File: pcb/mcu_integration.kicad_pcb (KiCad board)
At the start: 4 copper layers, 70 x 70 mm, 73 parts, among them IC1 TL7660IDGKR, IC2 TL081IDT, IC6 AD844_OPAMP_AL, IC7 FOD814_OPTO_AL, J1 Conn_01x05, J5 DM3BT-DSF-PEJS, M1 MountingHole_Pad, M2 MountingHole_Pad, M3 MountingHole_Pad, M4 MountingHole_Pad, U1 STM32F103RBTx, U2 LTC4300A-1IMS8_PBF, U3 REF192_AL, U6 LM35DM

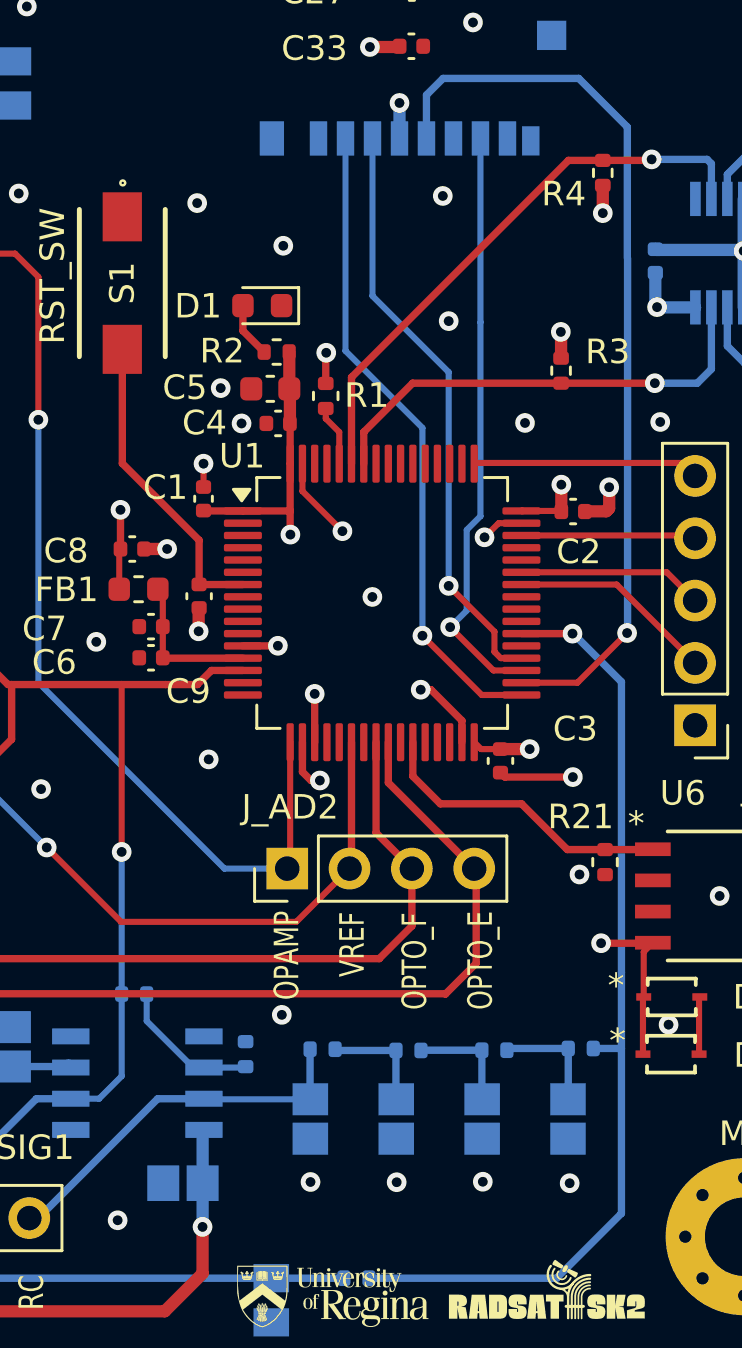
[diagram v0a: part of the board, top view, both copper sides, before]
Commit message: Added capacitor to op amp circuit
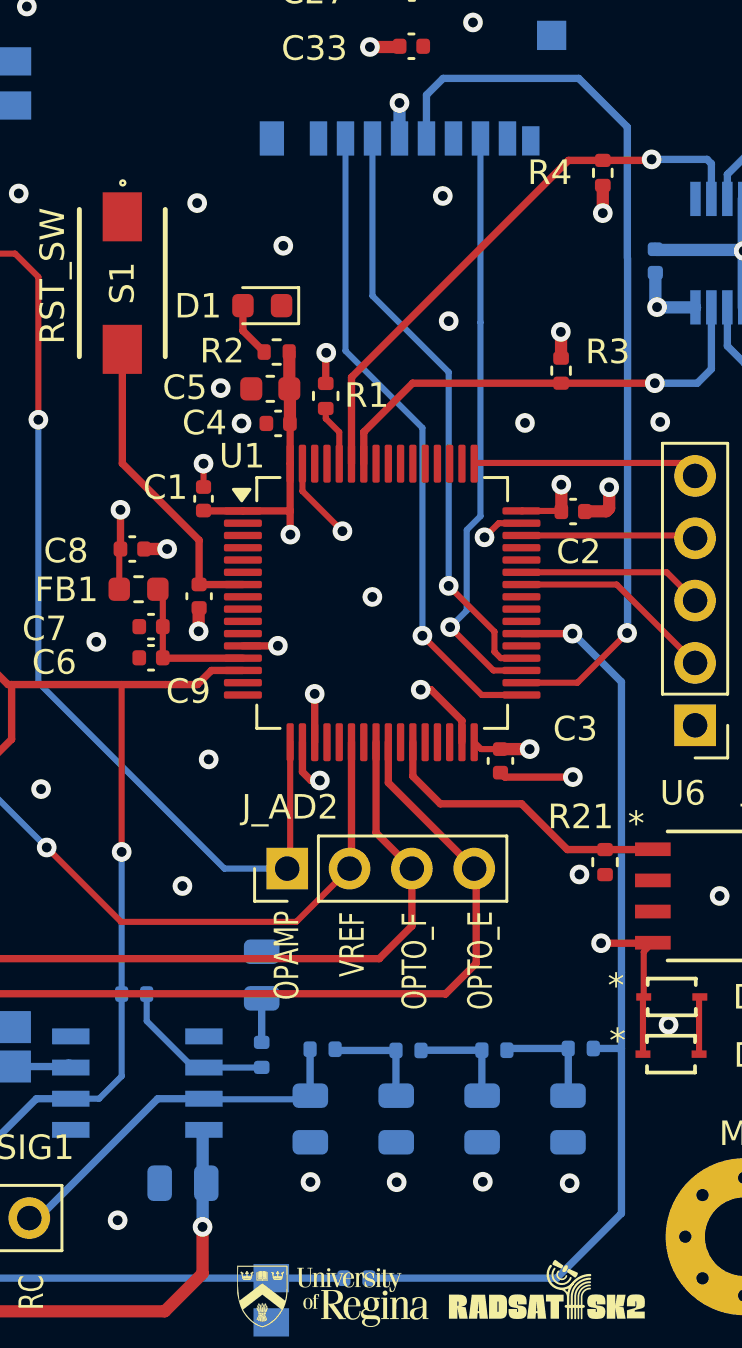
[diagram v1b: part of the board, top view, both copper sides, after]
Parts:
- added C47: 4.7u, Capacitor_SMD:C_0805_2012Metric, B.Cu at (153.6, 114.0)
- C14, C15, C16, C17, C18: footprint capstone:CAPC220145_88N_KEM-0.1u -> Capacitor_SMD:C_0805_2012Metric
- moved R9 0.66 mm to (153.6, 117.3)
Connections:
- R9 pad 2: GND -> Net-(C47-Pad1)
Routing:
- net Net-(C47-Pad1): track 0.00 -> 2.08 mm
- net Net-(IC2-INVERTING_INPUT): track 5.93 -> 6.52 mm
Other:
- board text added: "Minature Analog Payload REV B Owen Markewich Hunter Gerbrandt"
- board text removed: "Minature Analog Payload REV A Owen Markewich Hunter Gerbrandt"

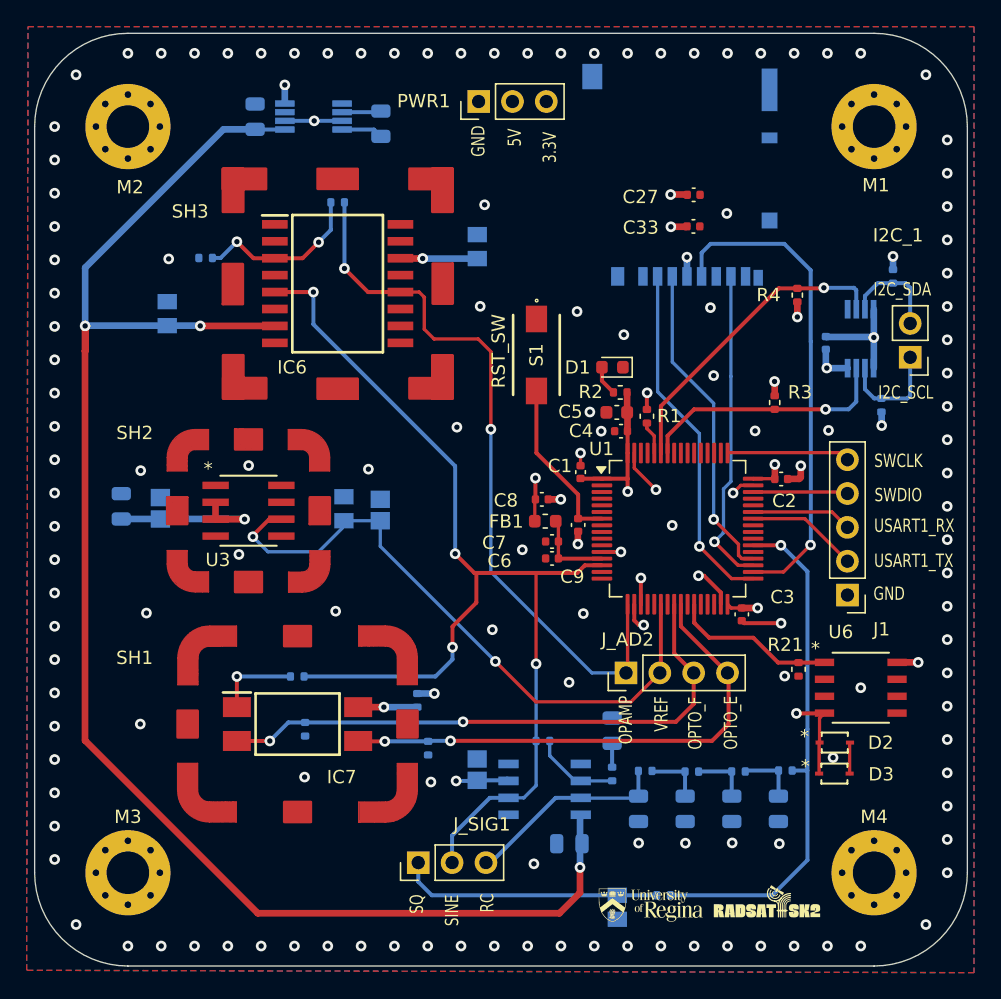
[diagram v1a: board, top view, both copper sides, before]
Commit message: Added switchable input for opto-coupler
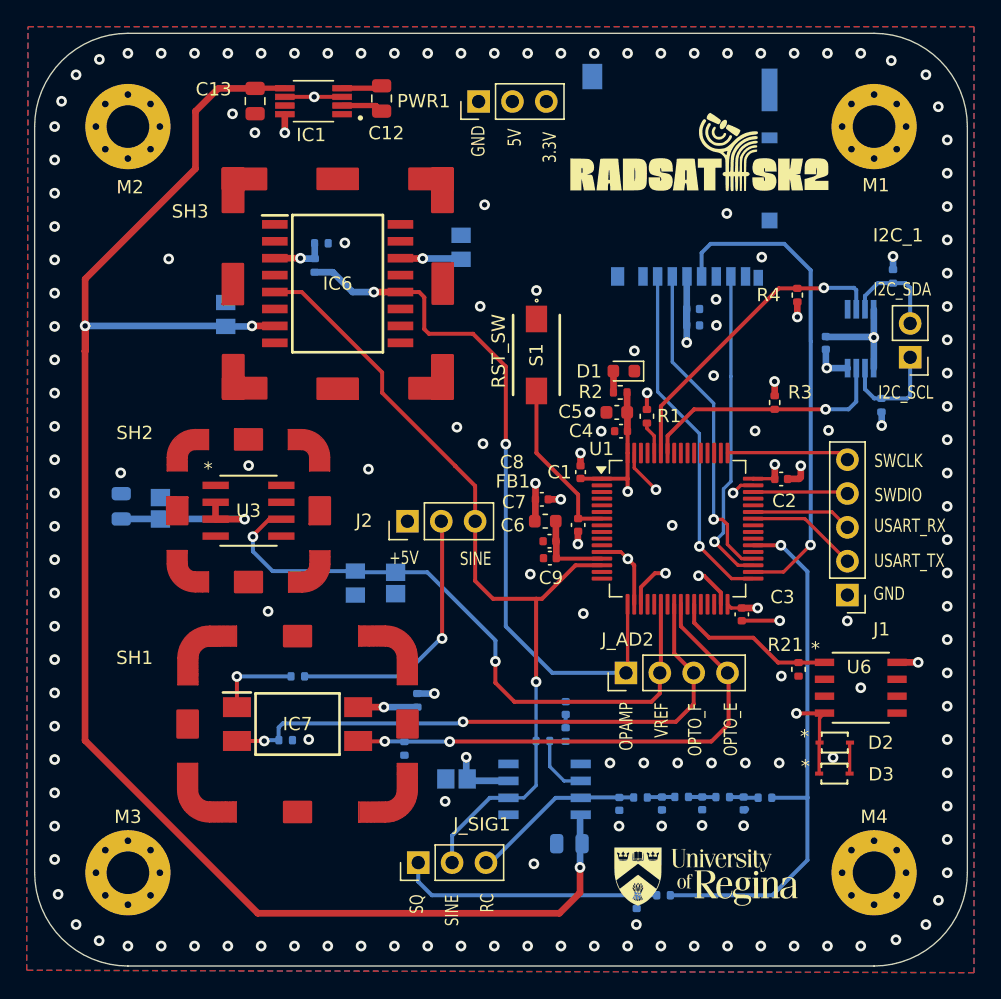
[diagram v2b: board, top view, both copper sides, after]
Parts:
- added G***: LOGO, LOGO, F.Cu at (160.0, 70.8)
- added G***: LOGO, LOGO, F.Cu at (160.6, 125.0)
- added J2: Conn_01x03, Connector_PinHeader_2.54mm:PinHeader_1x03_P2.54mm_Vertical, F.Cu at (138.2, 98.3)
- C12, C13, IC1: moved to F.Cu
- C14, C15, C16, C17, C47: footprint Capacitor_SMD:C_0805_2012Metric -> Capacitor_SMD:C_0402_1005Metric
- C27, C33: moved to B.Cu
- C43: footprint capstone:C0805 -> Capacitor_SMD:C_0402_1005Metric
- moved C27 9.80 mm to (159.6, 83.6)
- moved R22 8.76 mm to (131.7, 77.5), turned to 180 degrees
- moved C33 6.20 mm to (159.6, 82.4)
- moved C31 5.65 mm to (134.3, 103.0), turned to -90 degrees
- moved C32 5.59 mm to (137.3, 103.0), turned to -90 degrees
- moved R25 5.03 mm to (131.2, 79.1), turned to 90 degrees
- moved R9 4.58 mm to (150.1, 114.3)
- moved C29 4.39 mm to (124.6, 82.8)
- moved C47 3.87 mm to (150.1, 112.3)
- moved C14 2.64 mm to (163.4, 119.5)
- moved R5 2.55 mm to (165.0, 119.1)
- moved C15 2.26 mm to (160.3, 119.5)
- moved R6 2.25 mm to (161.9, 119.0)
- moved R7 2.05 mm to (158.8, 119.0)
- moved R8 2.02 mm to (155.7, 119.0)
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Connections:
- R23 pad 2: ADC1_IN0_SINE -> Net-(J2-Pin_2)
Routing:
- net Net-(J2-Pin_2): track 0.00 -> 20.6 mm, vias 0 -> 1
- net ADC1_IN0_SINE: track 84.6 -> 65.2 mm, vias 4 -> 1
- net Net-(IC6--IN): track 12.9 -> 4.16 mm, vias 2 -> 1
- net 3.3V Output: track 44.0 -> 48.2 mm, vias 13 -> 11
- net -5V Output: track 119.9 -> 123.2 mm
- net Net-(C14-Pad1): track 4.60 -> 2.17 mm
- net Net-(C15-Pad1): track 4.49 -> 2.06 mm
- net Net-(C16-Pad1): track 4.49 -> 2.09 mm
- net RC_OUTPUT: track 16.0 -> 13.8 mm
- net GND: track 35.3 -> 37.4 mm, vias 145 -> 161
- net SIG_SQUARE: track 39.1 -> 40.6 mm
- net ADC1_IN3_OPAMP_AL: track 55.8 -> 54.7 mm
- net Net-(C47-Pad1): track 2.08 -> 1.00 mm
- net ADC1_IN14_OPTO_F_AL: track 43.5 -> 44.2 mm
- net Net-(D1-A): track 2.25 -> 1.60 mm
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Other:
- board text added: "+5V"
- board text added: "USART_RX"
- board text added: "USART_TX"
- board text removed: "USART1_RX"
- board text removed: "USART1_TX"

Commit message: Changed IC test orientation
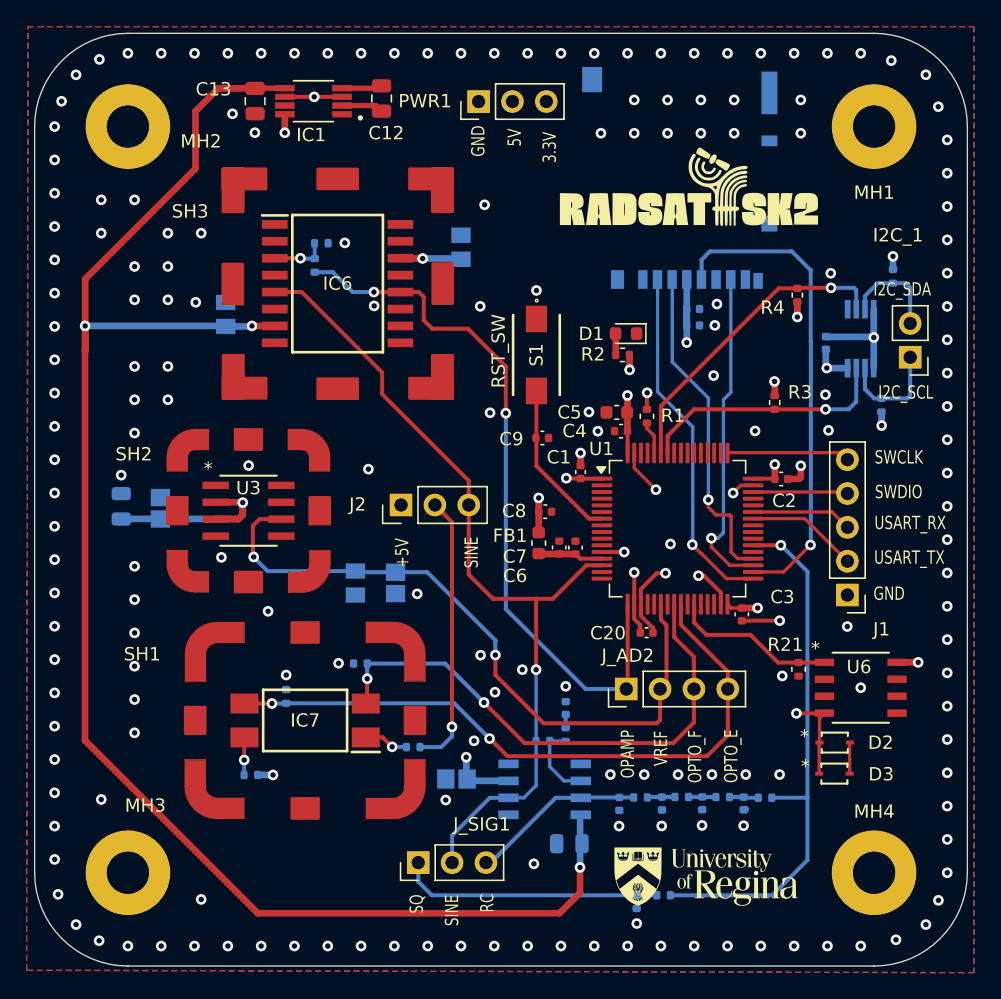
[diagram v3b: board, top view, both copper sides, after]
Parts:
- added C20: 100n, Capacitor_SMD:C_0402_1005Metric, F.Cu at (156.2, 106.7)
- MH1: renamed from M1; footprint MountingHole:MountingHole_3.2mm_M3_Pad_Via -> capstone:MountingHole_3.18mm_6.35mm_Pad
- MH2: renamed from M2; footprint MountingHole:MountingHole_3.2mm_M3_Pad_Via -> capstone:MountingHole_3.18mm_6.35mm_Pad
- MH3: renamed from M3; footprint MountingHole:MountingHole_3.2mm_M3_Pad_Via -> capstone:MountingHole_3.18mm_6.35mm_Pad
- MH4: renamed from M4; footprint MountingHole:MountingHole_3.2mm_M3_Pad_Via -> capstone:MountingHole_3.18mm_6.35mm_Pad
- moved R26 13.7 mm to (126.5, 117.4), turned to 0 degrees
- moved R23 10.2 mm to (138.6, 115.3)
- moved R27 9.69 mm to (129.1, 111.5), turned to -90 degrees
- moved R24 8.03 mm to (134.7, 109.0), turned to 180 degrees
- moved C9 7.06 mm to (148.3, 92.1), turned to 180 degrees
- moved D1 2.82 mm to (154.6, 84.2)
- moved R2 2.82 mm to (154.3, 85.8)
- moved G*** 2.71 mm to (159.2, 73.4)
- moved C6 2.08 mm to (150.8, 100.3), turned to 90 degrees
- moved FB1 1.72 mm to (148.1, 100.0), turned to 90 degrees
- moved J2 1.31 mm to (137.7, 97.1)
- moved J_AD2 1.21 mm to (154.6, 110.9)
- moved C8 0.96 mm to (148.5, 97.6)
- moved C7 0.87 mm to (149.6, 100.3), turned to 90 degrees
- moved IC7 0.63 mm to (130.5, 113.3), turned to 180 degrees
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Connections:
- net ADC1_IN8_VREG_MEL renamed ADC1_IN8
- net ADC1_IN9_VREG_AL renamed ADC1_IN9_LM35
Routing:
- net ADC1_IN15_OPTO_E_AL: track 39.0 -> 49.9 mm
- net ADC1_IN14_OPTO_F_AL: track 44.2 -> 40.1 mm
- net ADC1_IN6_VREF_AL: track 48.0 -> 51.1 mm
- net Net-(IC7-AK): track 6.36 -> 3.35 mm
- net +5V: track 26.4 -> 28.9 mm
- net Net-(IC7-C): track 4.44 -> 2.83 mm
- net Net-(U1-VDDA): track 6.35 -> 4.92 mm
- net GND: track 37.4 -> 36.1 mm, vias 161 -> 197
- net /SPI2_MISO: track 24.1 -> 24.9 mm
- net /SPI2_SCK: track 36.8 -> 36.1 mm
- net 3.3V Output: track 48.2 -> 47.5 mm, vias 11 -> 13
- net ADC1_IN3_OPAMP_AL: track 54.7 -> 55.3 mm
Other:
- board text added: "Minature Analog Payload REV B Hunter Gerbrandt Owen Markewich"
- board text removed: "Minature Analog Payload REV B Owen Markewich Hunter Gerbrandt"

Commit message: Thermal Reliefs for Shields
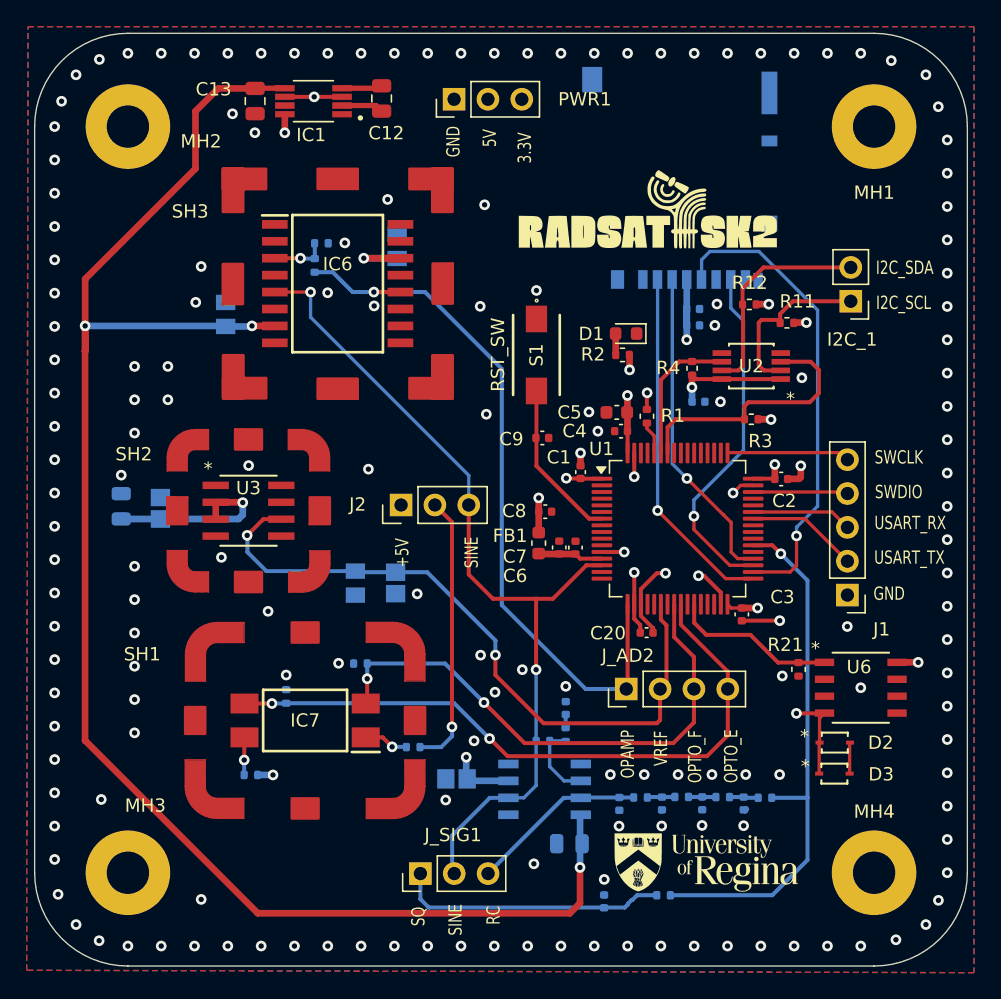
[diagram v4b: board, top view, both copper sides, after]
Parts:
- R11, R12, U2: moved to F.Cu
- moved R12 11.0 mm to (163.9, 82.0), turned to 180 degrees
- moved C19 10.5 mm to (160.0, 89.3), turned to 180 degrees
- moved R4 9.62 mm to (159.6, 86.8)
- moved R11 9.41 mm to (166.7, 83.4), turned to 180 degrees
- moved U2 8.46 mm to (164.0, 86.7), turned to 180 degrees
- moved I2C_1 6.13 mm to (171.5, 81.8)
- moved C30 4.80 mm to (137.4, 77.7)
- moved G*** 3.52 mm to (156.2, 75.1)
- moved C43 2.44 mm to (153.0, 126.8), turned to -90 degrees
- moved R3 2.16 mm to (164.0, 90.7), turned to 180 degrees
- moved PWR1 1.85 mm to (141.7, 66.7)
- moved G*** 1.06 mm to (160.6, 123.9)
- moved J_SIG1 0.84 mm to (139.2, 124.8)
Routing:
- net OBC_I2C_SDA: track 23.4 -> 10.6 mm, vias 1 -> 0
- net I2C_SDA: track 7.61 -> 16.1 mm
- net I2C_SCL: track 8.23 -> 13.2 mm
- net GND: track 36.1 -> 31.4 mm, vias 197 -> 175
- net 3.3V Output: track 47.5 -> 50.0 mm, vias 13 -> 12
- net /SPI2_MISO: track 24.9 -> 26.3 mm
- net +5V: track 28.9 -> 27.9 mm
- net OBC_I2C_SCL: track 19.0 -> 19.8 mm, vias 1 -> 0
- net /SPI2_SCK: track 36.1 -> 35.3 mm
- net ADC1_IN3_OPAMP_AL: track 55.3 -> 56.0 mm, vias 2 -> 1
- net /SPI2_MOSI: track 25.0 -> 24.4 mm
- net Net-(J_SIG1-Pin_1): track 19.8 -> 20.4 mm
- net ADC1_IN0_SINE: track 65.2 -> 64.9 mm, vias 1 -> 2

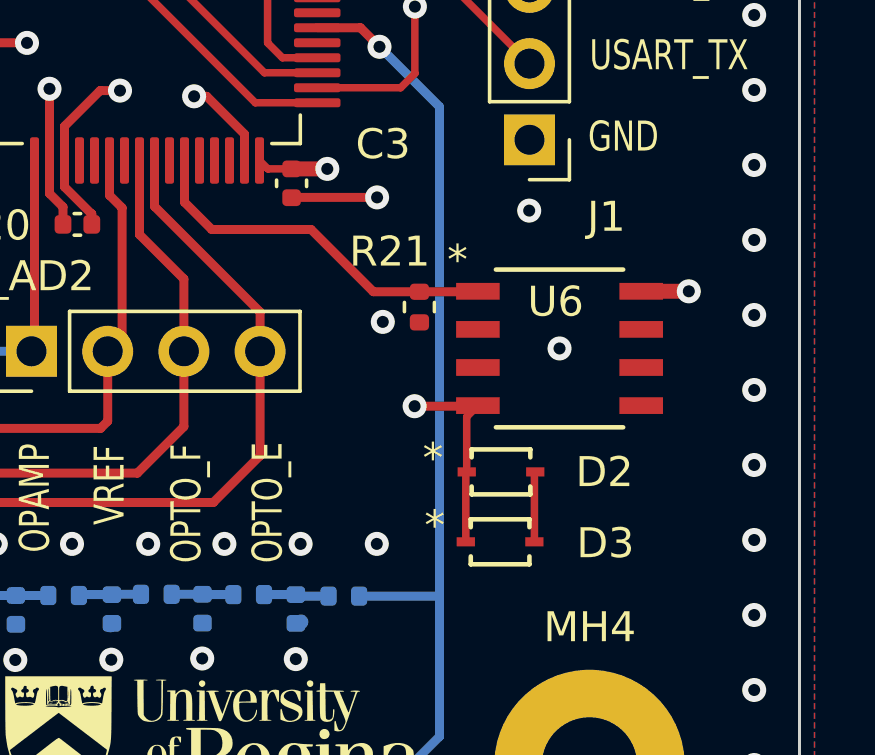
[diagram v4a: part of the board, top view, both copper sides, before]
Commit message: Replaced LM35 temp sensor with LMT87
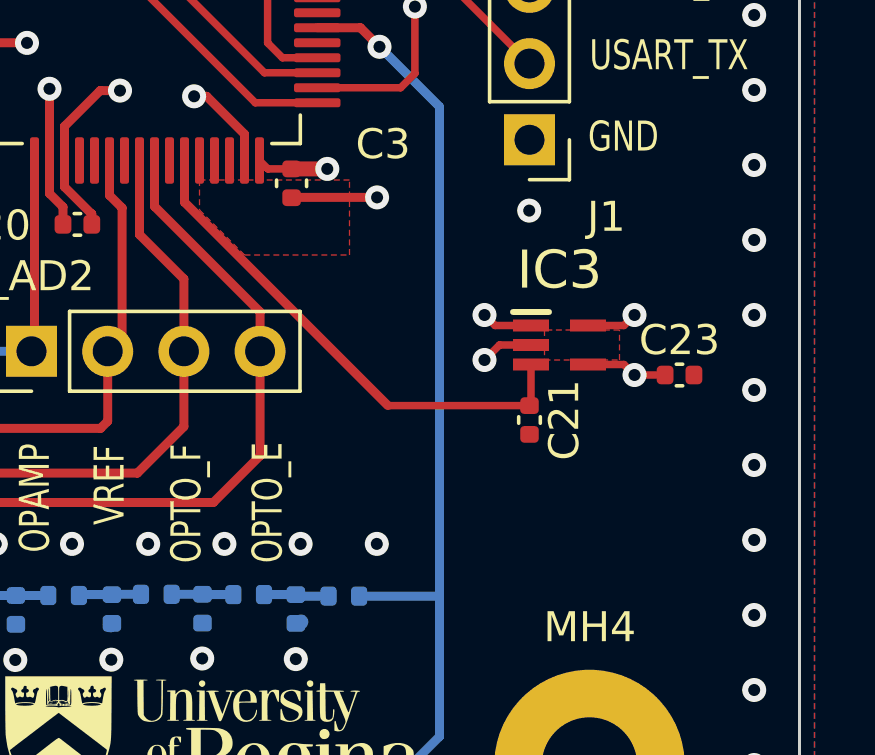
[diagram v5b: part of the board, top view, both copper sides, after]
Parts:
- removed D2, D3: 1N914, capstone:SOD-323_1P7X1P25_ONS
- removed R21: 18K, Resistor_SMD:R_0402_1005Metric
- removed U6: LM35DM, capstone:LM35DM
- added C21: 0.22n, Capacitor_SMD:C_0402_1005Metric, F.Cu at (171.2, 113.2)
- added C23: 0.01u, Capacitor_SMD:C_0402_1005Metric, F.Cu at (176.2, 111.7)
- added IC3: LMT87DCKT, SamacSys_Parts:SOT65P210X110-5N, F.Cu at (172.2, 110.7)
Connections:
- U1 pad 27: ADC1_IN9_LM35 -> ADC1_IN9_LMT87
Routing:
- net ADC1_IN9_LMT87: track 0.00 -> 17.1 mm
- net ADC1_IN9_LM35: track 12.4 -> 0.00 mm
- net GND: track 31.4 -> 26.3 mm, vias 175 -> 173
- net +5V: track 27.9 -> 32.4 mm, vias 6 -> 8
- net DIODE_NET: track 2.34 -> 0.00 mm
- removed copper zone on In1.Cu, net GND
